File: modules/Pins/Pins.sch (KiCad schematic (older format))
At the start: 25 parts, among them J1 2, J10 11, J11 12, J12 13, J13 A0, J14 A1, J15 A2, J16 A3, J17 A4, J18 A5, J19 Vcc, J2 3, J20 Gnd, J21 Conn_01x10_Male, J3 4, J4 5, J5 6, J6 7, J7 8, J8 9, J9 10

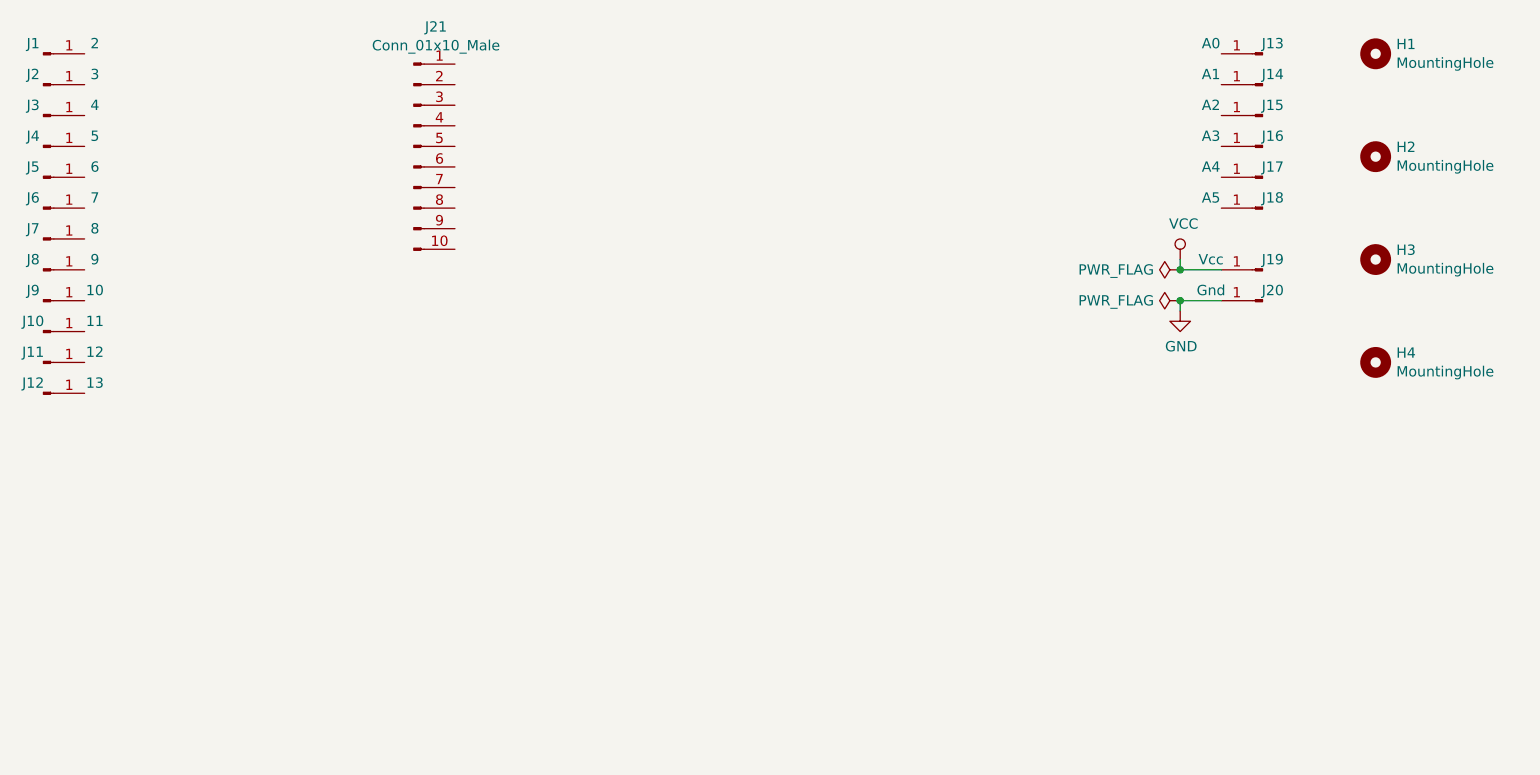
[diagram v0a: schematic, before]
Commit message: Add some pinheaders
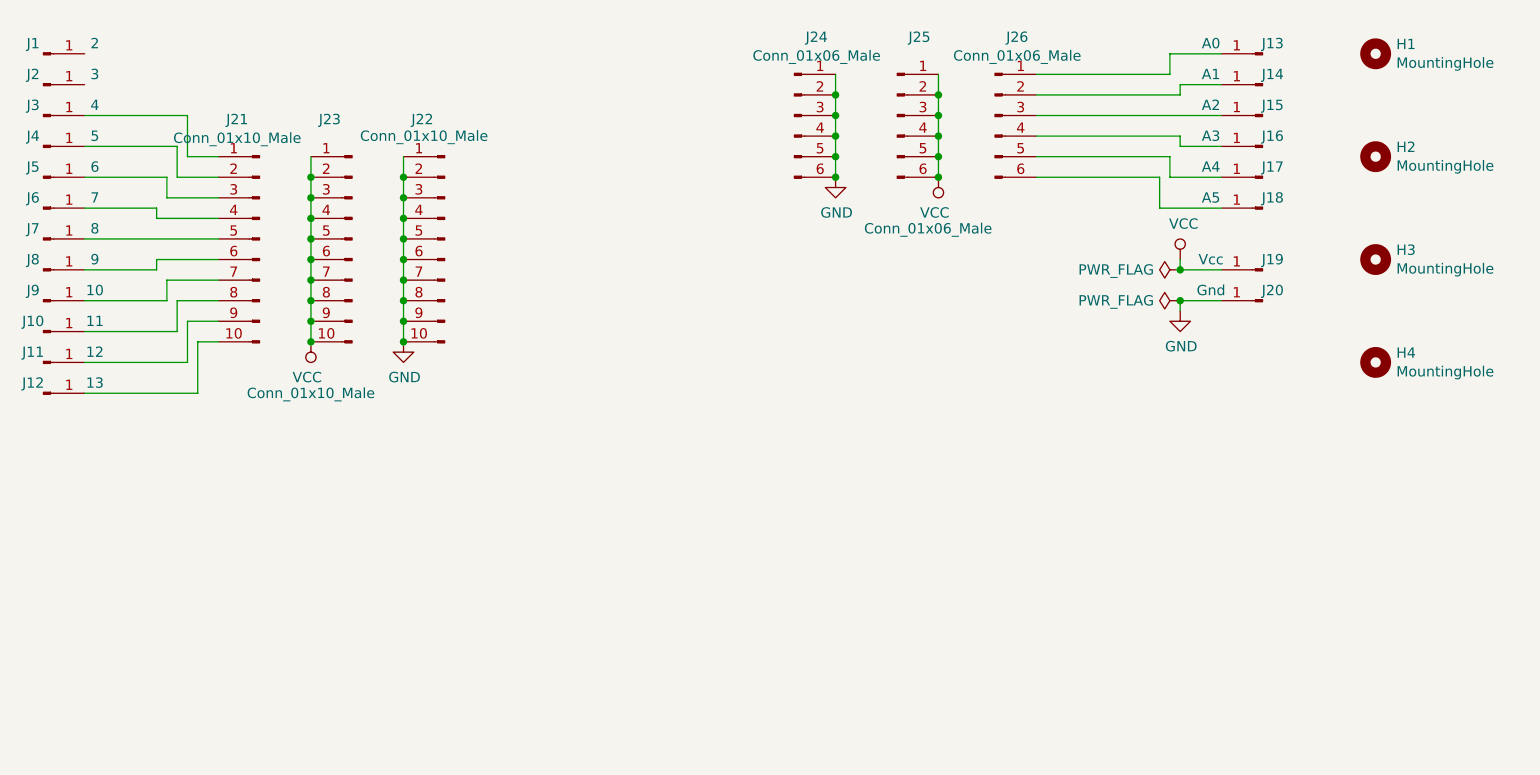
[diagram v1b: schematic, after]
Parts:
- added J22, J23: Conn_01x10_Male, Connector_PinHeader_2.54mm:PinHeader_1x10_P2.54mm_Vertical, symbol Connector:Conn_01x10_Male
- added J24, J25, J26: Conn_01x06_Male, Connector_PinHeader_2.54mm:PinHeader_1x06_P2.54mm_Vertical, symbol Connector:Conn_01x06_Male
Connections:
- net GND: now also J22.1 (Pin_1), J22.10 (Pin_10), J22.2 (Pin_2), J22.3 (Pin_3), J22.4 (Pin_4), J22.5 (Pin_5), J22.6 (Pin_6), J22.7 (Pin_7), J22.8 (Pin_8), J22.9 (Pin_9), J24.1 (Pin_1), J24.2 (Pin_2), J24.3 (Pin_3), J24.4 (Pin_4), J24.5 (Pin_5), J24.6 (Pin_6)
- net VCC: now also J23.1 (Pin_1), J23.10 (Pin_10), J23.2 (Pin_2), J23.3 (Pin_3), J23.4 (Pin_4), J23.5 (Pin_5), J23.6 (Pin_6), J23.7 (Pin_7), J23.8 (Pin_8), J23.9 (Pin_9), J25.1 (Pin_1), J25.2 (Pin_2), J25.3 (Pin_3), J25.4 (Pin_4), J25.5 (Pin_5), J25.6 (Pin_6)
- net at J3.1 (Pin_1): now also J21.1 (Pin_1)
- net at J4.1 (Pin_1): now also J21.2 (Pin_2)
- net at J5.1 (Pin_1): now also J21.3 (Pin_3)
- net at J6.1 (Pin_1): now also J21.4 (Pin_4)
- net at J7.1 (Pin_1): now also J21.5 (Pin_5)
- net at J8.1 (Pin_1): now also J21.6 (Pin_6)
- net at J9.1 (Pin_1): now also J21.7 (Pin_7)
- net at J10.1 (Pin_1): now also J21.8 (Pin_8)
- net at J11.1 (Pin_1): now also J21.9 (Pin_9)
- net at J13.1 (Pin_1): now also J26.1 (Pin_1)
- net at J14.1 (Pin_1): now also J26.2 (Pin_2)
- net at J15.1 (Pin_1): now also J26.3 (Pin_3)
- net at J16.1 (Pin_1): now also J26.4 (Pin_4)
- net at J17.1 (Pin_1): now also J26.5 (Pin_5)
- net at J18.1 (Pin_1): now also J26.6 (Pin_6)
- net at J12.1 (Pin_1): now also J21.10 (Pin_10)
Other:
- moved on the sheet: J21

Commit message: Pins (sensor) shield ready
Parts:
- removed J21, J22, J23: Conn_01x10_Male, Connector_PinHeader_2.54mm:PinHeader_1x10_P2.54mm_Vertical, symbol Connector:Conn_01x10_Male
- added J21, J22, J23: Conn_01x12_Male, Connector_PinHeader_2.54mm:PinHeader_1x12_P2.54mm_Vertical, symbol Connector:Conn_01x12_Male
- added J27, J28, J29: Conn_01x04_Male, Connector_PinHeader_2.54mm:PinHeader_1x04_P2.54mm_Vertical, symbol Connector:Conn_01x04_Male
- added J30, J31: Conn_01x06_Male, Connector_PinHeader_2.54mm:PinHeader_1x06_P2.54mm_Vertical, symbol Connector:Conn_01x06_Male
- added JP1: Jumper_3_Bridged12, Connector_PinHeader_2.54mm:PinHeader_1x03_P2.54mm_Vertical, symbol Jumper:Jumper_3_Bridged12
- added RN1: R_Network06, Resistor_THT:R_Array_SIP7, symbol Device:R_Network06
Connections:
- net GND: now also J23.1 (Pin_1), J23.10 (Pin_10), J23.11 (Pin_11), J23.12 (Pin_12), J23.2 (Pin_2), J23.3 (Pin_3), J23.4 (Pin_4), J23.5 (Pin_5), J23.6 (Pin_6), J23.7 (Pin_7), J23.8 (Pin_8), J23.9 (Pin_9), J27.4 (Pin_4), J28.4 (Pin_4), J29.4 (Pin_4), JP1.3 (B)
- net VCC: now also J22.1 (Pin_1), J22.10 (Pin_10), J22.11 (Pin_11), J22.12 (Pin_12), J22.2 (Pin_2), J22.3 (Pin_3), J22.4 (Pin_4), J22.5 (Pin_5), J22.6 (Pin_6), J22.7 (Pin_7), J22.8 (Pin_8), J22.9 (Pin_9), J27.3 (Pin_3), J28.3 (Pin_3), J29.3 (Pin_3), JP1.1 (A)
- net at J1.1 (Pin_1): now also J21.1 (Pin_1)
- net at J2.1 (Pin_1): now also J21.2 (Pin_2)
- net at J3.1 (Pin_1): now also J21.3 (Pin_3)
- net at J4.1 (Pin_1): now also J21.4 (Pin_4)
- net at J5.1 (Pin_1): now also J21.5 (Pin_5)
- net at J6.1 (Pin_1): now also J21.6 (Pin_6)
- net at J7.1 (Pin_1): now also J21.7 (Pin_7)
- net at J8.1 (Pin_1): now also J21.8 (Pin_8)
- net at J9.1 (Pin_1): now also J21.9 (Pin_9)
- net at J10.1 (Pin_1): now also J21.10 (Pin_10)
- net at J11.1 (Pin_1): now also J21.11 (Pin_11)
- net SDA: now reaches J17.1 (Pin_1), J26.5 (Pin_5)
- net SDA: now also J27.2 (Pin_2), J28.2 (Pin_2), J29.2 (Pin_2)
- net SCL: now reaches J18.1 (Pin_1), J26.6 (Pin_6)
- net SCL: now also J27.1 (Pin_1), J28.1 (Pin_1), J29.1 (Pin_1)
- net at J12.1 (Pin_1): now also J21.12 (Pin_12)
- new net: JP1.2 (C), RN1.1 (common)
- new net: J30.1 (Pin_1), J31.1 (Pin_1), RN1.2 (R1)
- new net: J30.2 (Pin_2), J31.2 (Pin_2), RN1.3 (R2)
- new net: J30.3 (Pin_3), J31.3 (Pin_3), RN1.4 (R3)
- new net: J30.4 (Pin_4), J31.4 (Pin_4), RN1.5 (R4)
- new net: J30.5 (Pin_5), J31.5 (Pin_5), RN1.6 (R5)
- new net: J30.6 (Pin_6), J31.6 (Pin_6), RN1.7 (R6)
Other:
- note added: "I2C"
